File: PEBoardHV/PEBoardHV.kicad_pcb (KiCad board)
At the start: 2 copper layers, 106.7 x 76.7 mm, 44 parts, among them J1 To PE LV, J2 Left Connector (Master), J3 E-Meter Internal, J4 Right Connector (Slave), J5 E-Meter External, J6 HV Cable, J7 TSMPs, J8 HV CAN Debug, J9 EMeter HV, U1 L78S05CV-DG, U2 ISO1050, U3 PS2501-4, U4 DK1A1B-12V, U5 DK1A1B-12V

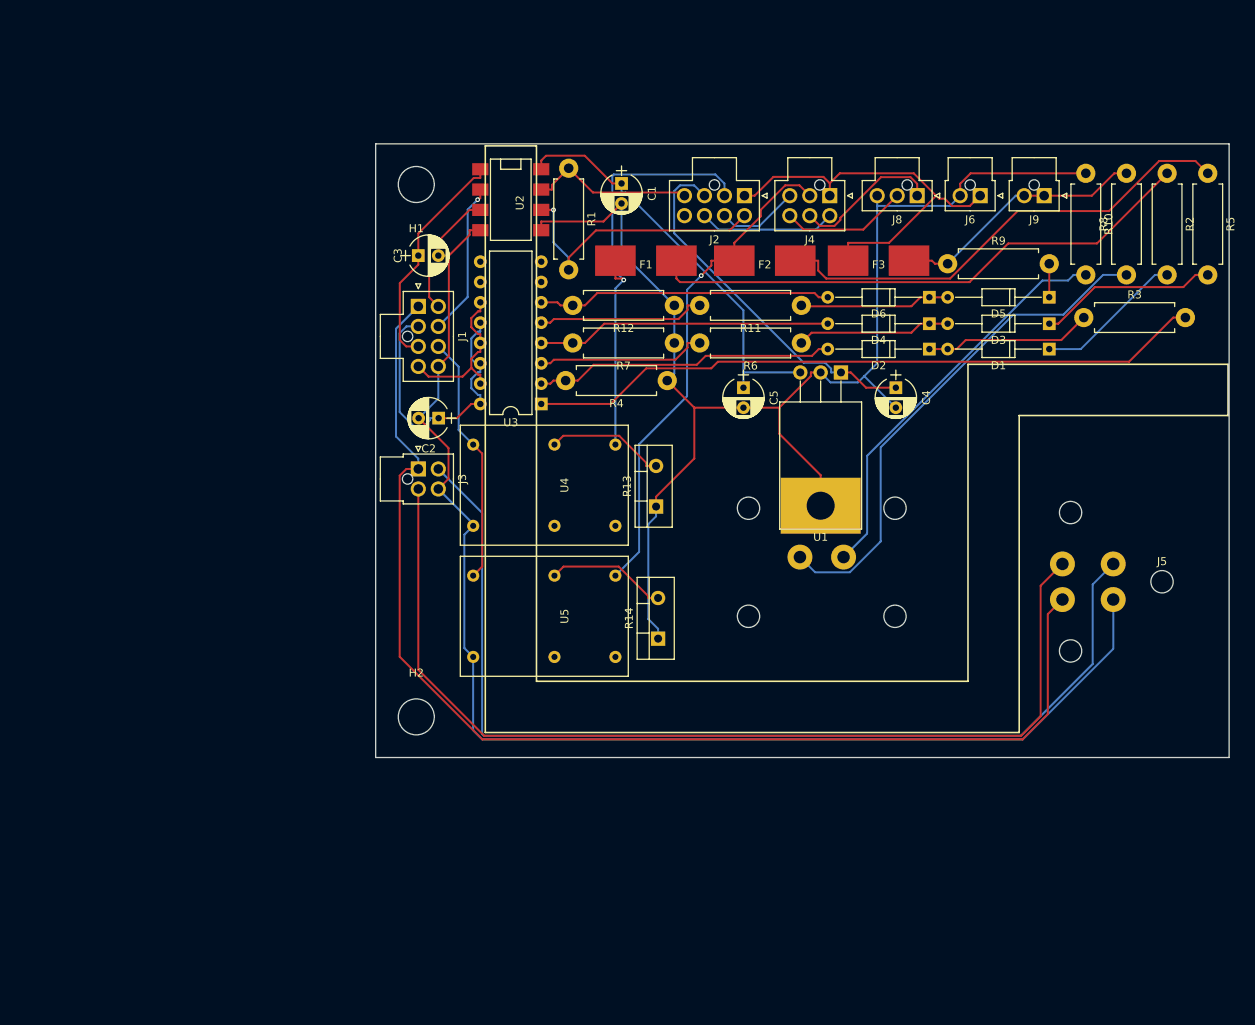
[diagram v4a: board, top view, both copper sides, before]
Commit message: Add ground planes to PE HV PCB and add an additional mounting hole
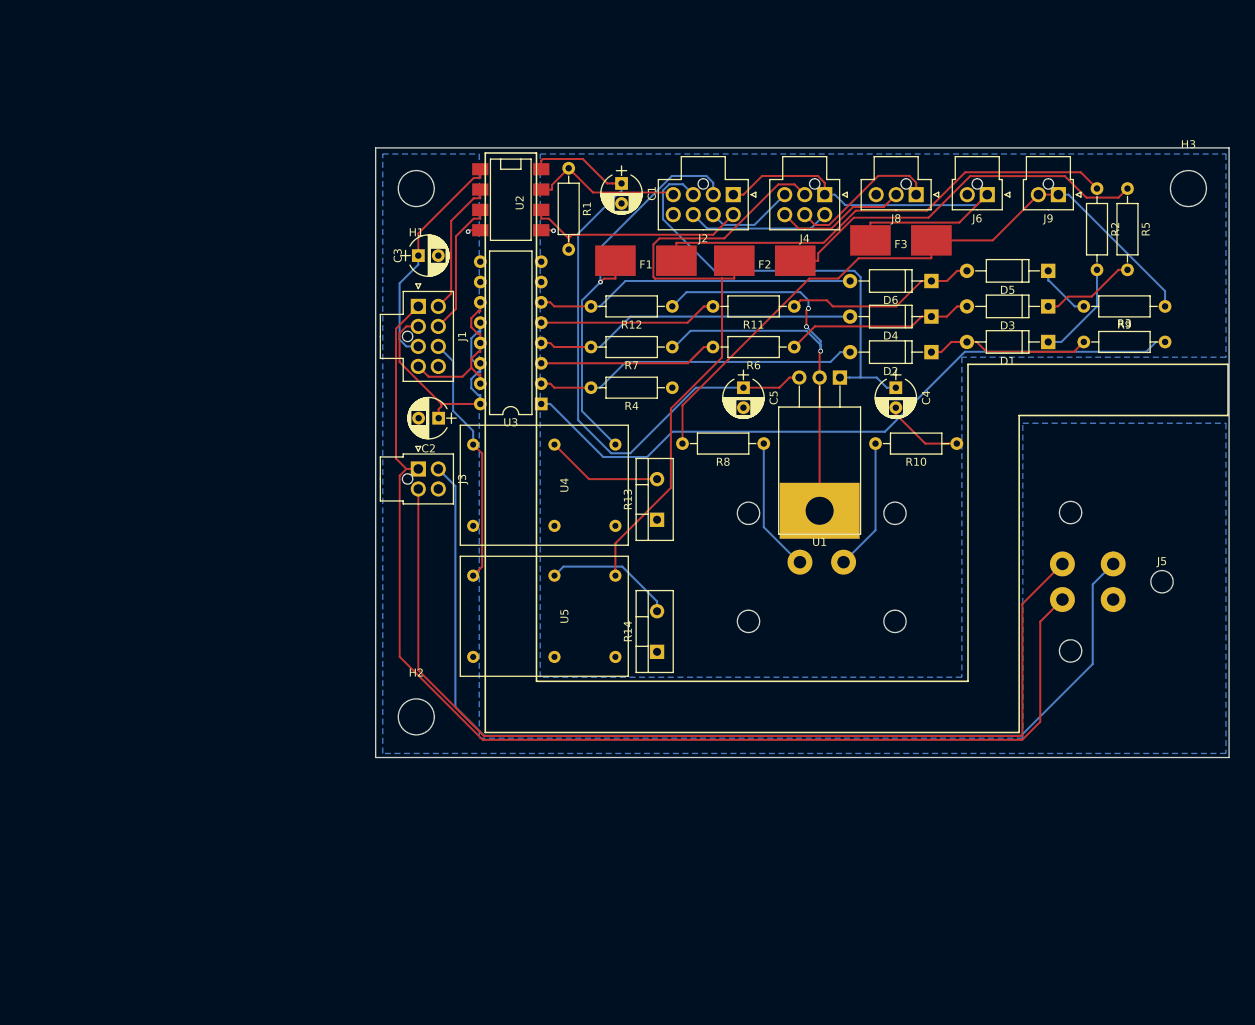
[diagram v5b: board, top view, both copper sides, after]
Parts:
- added H3: MtngHole, Mounting_Holes:MountingHole_4.5mm, F.Cu at (222.0, 56.4)
- D1, D2, D3, D4, D5, D6: footprint Diodes_THT:D_DO-35_SOD27_P12.70mm_Horizontal -> Diodes_THT:D_A-405_P10.16mm_Horizontal
- R1, R10, R11, R12, R2, R3, R4, R5, R6, R7, R8, R9: footprint Resistors_THT:R_Axial_DIN0411_L9.9mm_D3.6mm_P12.70mm_Horizontal -> Resistors_THT:R_Axial_DIN0207_L6.3mm_D2.5mm_P10.16mm_Horizontal
- moved R8 50.0 mm to (168.9, 88.3), turned to 180 degrees
- moved R10 37.4 mm to (193.0, 88.3), turned to 180 degrees
- moved R9 27.7 mm to (219.1, 71.1), turned to 180 degrees
- moved R5 10.2 mm to (214.4, 56.4)
- moved R2 8.97 mm to (210.6, 56.4)
- moved F3 3.78 mm to (186.1, 62.9)
- moved D5 3.30 mm to (204.5, 66.7)
- moved R3 3.05 mm to (208.9, 75.6)
- moved D3 2.16 mm to (204.5, 71.1)
- moved D6 2.05 mm to (189.9, 67.9)
- moved J9 1.78 mm to (205.7, 57.1)
- moved R13 1.66 mm to (155.6, 97.8)
- moved R14 1.66 mm to (155.6, 114.3)
- moved J2 1.40 mm to (165.1, 57.1)
- moved R4 1.09 mm to (157.5, 81.3)
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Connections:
- J1 pad 5: /CAN_TX -> /CAN_RX
- J1 pad 6: /CAN_RX -> /CAN_TX
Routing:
- net GND: track 163.9 -> 1.59 mm, vias 0 -> 1
- net /TS-: track 169.9 -> 77.8 mm, vias 0 -> 4
- net /TS+_FUSED: track 32.0 -> 84.2 mm
- net Net-(J7-Pad1): track 63.9 -> 16.8 mm
- net Net-(J7-Pad2): track 50.6 -> 16.5 mm
- net /5V_TS: track 52.1 -> 77.8 mm
- net /TS+_SWITCHED_R: track 62.9 -> 81.7 mm, vias 1 -> 0
- net Net-(F2-Pad2): track 59.9 -> 48.0 mm
- net Net-(D3-Pad1): track 22.3 -> 11.8 mm
- net /CAN+: track 45.9 -> 56.0 mm
- net Net-(F1-Pad2): track 69.4 -> 59.3 mm
- net /CAN_L_BOARD: track 35.5 -> 28.7 mm, vias 1 -> 0
- net Net-(D1-Pad1): track 18.6 -> 12.5 mm
- net Net-(D5-Pad2): track 18.8 -> 24.1 mm
- net Net-(D3-Pad2): track 19.3 -> 23.7 mm
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- added copper zone on B.Cu, net /TS-
- added copper zone on B.Cu, net GND
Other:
- board size 106.7 x 76.7 mm -> 106.7 x 76.2 mm

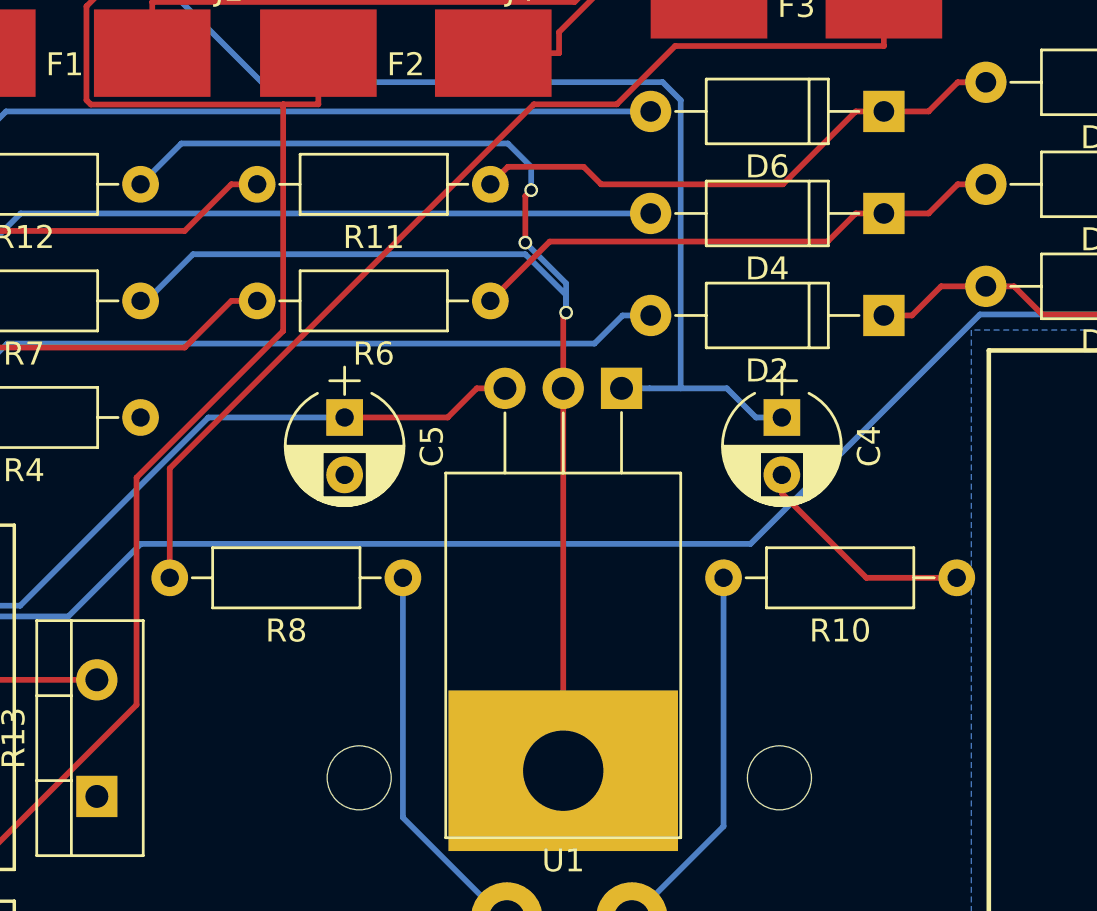
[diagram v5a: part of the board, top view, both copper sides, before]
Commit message: Fix via size for manufacturing
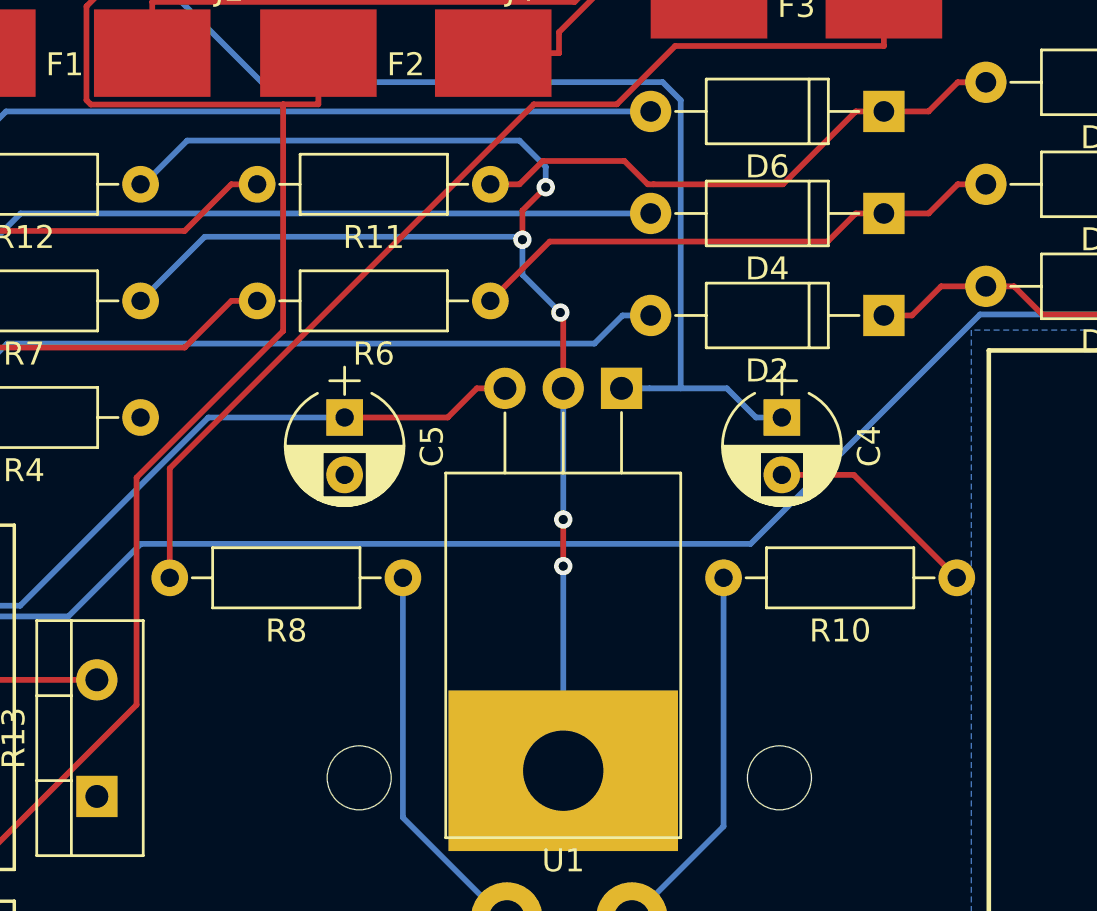
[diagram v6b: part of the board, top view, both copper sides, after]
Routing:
- net /TS-: track 77.8 -> 75.3 mm, vias 4 -> 6
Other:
- net class Default: via_dia 0.6 -> 0.8
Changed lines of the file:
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@@
     (links 85)
     (no_connects 0)
-    (area 120.345999 50.749999 227.126001 127.558001)
+    (area 120.345999 49.913 227.349001 129.003)
     (thickness 1.6)
     (drawings 14)
-    (tracks 328)
+    (tracks 332)
     (zones 0)
     (modules 45)
@@
     (segment_width 0.2)
     (edge_width 0.1)
-    (via_size 0.6)
+    (via_size 0.8)
     (via_drill 0.4)
     (via_min_size 0.4)
@@
     (clearance 0.2)
     (trace_width 0.25)
-    (via_dia 0.6)
+    (via_dia 0.8)
     (via_drill 0.4)
     (uvia_dia 0.3)
@@
   (segment (start 184.2947 81.28) (end 183.0247 80.01) (width 0.25) (layer B.Cu) (net 4))
   (segment (start 181.0133 80.01) (end 179.6603 80.01) (width 0.25) (layer B.Cu) (net 4))
-  (segment (start 157.48 71.12) (end 159.258 69.342) (width 0.25) (layer B.Cu) (net 5))
-  (segment (start 176.022 75.438) (end 176.022 76.708) (width 0.25) (layer B.Cu) (net 5))
-  (segment (start 174.244 73.66) (end 176.022 75.438) (width 0.25) (layer B.Cu) (net 5))
-  (via (at 174.244 73.66) (size 0.6) (drill 0.4) (layers F.Cu B.Cu) (net 5))
-  (segment (start 174.244 71.628) (end 174.244 73.66) (width 0.25) (layer F.Cu) (net 5))
-  (segment (start 174.498 71.374) (end 174.244 71.628) (width 0.25) (layer F.Cu) (net 5))
-  (via (at 174.498 71.374) (size 0.6) (drill 0.4) (layers F.Cu B.Cu) (net 5))
-  (segment (start 174.498 70.358) (end 174.498 71.374) (width 0.25) (layer B.Cu) (net 5))
-  (segment (start 173.482 69.342) (end 174.498 70.358) (width 0.25) (layer B.Cu) (net 5))
-  (segment (start 159.258 69.342) (end 173.482 69.342) (width 0.25) (layer B.Cu) (net 5))
-  (segment (start 157.48 76.2) (end 157.734 76.2) (width 0.25) (layer B.Cu) (net 5))
-  (segment (start 157.734 76.2) (end 159.766 74.168) (width 0.25) (layer B.Cu) (net 5))
-  (segment (start 159.766 74.168) (end 174.244 74.168) (width 0.25) (layer B.Cu) (net 5))
-  (segment (start 174.244 74.168) (end 176.022 75.946) (width 0.25) (layer B.Cu) (net 5))
-  (segment (start 176.022 75.946) (end 176.022 76.708) (width 0.25) (layer B.Cu) (net 5))
-  (via (at 176.022 76.708) (size 0.6) (drill 0.4) (layers F.Cu B.Cu) (net 5))
-  (segment (start 176.022 76.708) (end 175.895 76.835) (width 0.25) (layer F.Cu) (net 5))
-  (segment (start 175.895 76.835) (end 175.895 80.01) (width 0.25) (layer F.Cu) (net 5))
-  (segment (start 175.895 80.01) (end 175.895 96.67) (width 0.25) (layer F.Cu) (net 5))
-  (segment (start 185.42 83.78) (end 185.42 84.582) (width 0.25) (layer F.Cu) (net 5))
-  (segment (start 189.103 88.265) (end 193.04 88.265) (width 0.25) (layer F.Cu) (net 5))
-  (segment (start 185.42 84.582) (end 189.103 88.265) (width 0.25) (layer F.Cu) (net 5))
+  (segment (start 175.895 80.01) (end 175.895 76.835) (width 0.25) (layer F.Cu) (net 5) (status 400000))
+  (segment (start 174.117 75.057) (end 174.117 73.533) (width 0.25) (layer B.Cu) (net 5))
+  (segment (start 175.768 76.708) (end 174.117 75.057) (width 0.25) (layer B.Cu) (net 5))
+  (via (at 175.768 76.708) (size 0.8) (drill 0.4) (layers F.Cu B.Cu) (net 5))
+  (segment (start 175.895 76.835) (end 175.768 76.708) (width 0.25) (layer F.Cu) (net 5))
+  (segment (start 157.48 71.12) (end 157.607 71.12) (width 0.25) (layer B.Cu) (net 5) (status C00000))
+  (segment (start 157.607 71.12) (end 159.512 69.215) (width 0.25) (layer B.Cu) (net 5) (status 400000))
+  (via (at 174.117 73.533) (size 0.8) (drill 0.4) (layers F.Cu B.Cu) (net 5))
+  (segment (start 174.117 72.263) (end 174.117 73.533) (width 0.25) (layer F.Cu) (net 5))
+  (segment (start 175.133 71.247) (end 174.117 72.263) (width 0.25) (layer F.Cu) (net 5))
+  (via (at 175.133 71.247) (size 0.8) (drill 0.4) (layers F.Cu B.Cu) (net 5))
+  (segment (start 175.133 70.358) (end 175.133 71.247) (width 0.25) (layer B.Cu) (net 5))
+  (segment (start 173.99 69.215) (end 175.133 70.358) (width 0.25) (layer B.Cu) (net 5))
+  (segment (start 159.512 69.215) (end 173.99 69.215) (width 0.25) (layer B.Cu) (net 5))
+  (segment (start 174.117 73.533) (end 173.99 73.406) (width 0.25) (layer B.Cu) (net 5))
+  (segment (start 160.274 73.406) (end 157.48 76.2) (width 0.25) (layer B.Cu) (net 5) (status 800000))
+  (segment (start 173.99 73.406) (end 160.274 73.406) (width 0.25) (layer B.Cu) (net 5))
+  (segment (start 175.895 96.67) (end 175.895 87.757) (width 0.25) (layer B.Cu) (net 5) (status 400000))
+  (segment (start 175.895 85.725) (end 175.895 80.01) (width 0.25) (layer B.Cu) (net 5) (status 800000))
+  (via (at 175.895 85.725) (size 0.8) (drill 0.4) (layers F.Cu B.Cu) (net 5))
+  (segment (start 175.895 87.757) (end 175.895 85.725) (width 0.25) (layer F.Cu) (net 5))
+  (via (at 175.895 87.757) (size 0.8) (drill 0.4) (layers F.Cu B.Cu) (net 5))
+  (segment (start 185.42 83.78) (end 188.555 83.78) (width 0.25) (layer F.Cu) (net 5) (status 400000))
+  (segment (start 188.555 83.78) (end 193.04 88.265) (width 0.25) (layer F.Cu) (net 5) (status 800000))
   (via (at 142.6362 61.6604) (size 0.6) (layers F.Cu B.Cu) (net 5))
   (segment (start 141.097 61.595) (end 142.4383 61.595) (width 0.25) (layer F.Cu) (net 5))
@@
   (segment (start 208.915 71.12) (end 207.7897 71.12) (width 0.25) (layer B.Cu) (net 13))
   (segment (start 204.47 66.675) (end 204.47 67.9003) (width 0.25) (layer B.Cu) (net 13))
-  (segment (start 172.72 71.12) (end 173.482 70.358) (width 0.25) (layer F.Cu) (net 14))
-  (segment (start 176.784 70.358) (end 177.546 71.12) (width 0.25) (layer F.Cu) (net 14))
-  (segment (start 173.482 70.358) (end 176.784 70.358) (width 0.25) (layer F.Cu) (net 14))
+  (segment (start 173.99 71.12) (end 175.006 70.104) (width 0.25) (layer F.Cu) (net 14))
+  (segment (start 179.578 71.12) (end 179.832 71.12) (width 0.25) (layer F.Cu) (net 14))
+  (segment (start 178.562 70.104) (end 179.578 71.12) (width 0.25) (layer F.Cu) (net 14))
+  (segment (start 175.006 70.104) (end 178.562 70.104) (width 0.25) (layer F.Cu) (net 14))
   (segment (start 191.8147 67.945) (end 193.0847 66.675) (width 0.25) (layer F.Cu) (net 14))
   (segment (start 189.865 67.945) (end 191.8147 67.945) (width 0.25) (layer F.Cu) (net 14))
   (segment (start 194.31 66.675) (end 193.0847 66.675) (width 0.25) (layer F.Cu) (net 14))
   (segment (start 185.4647 71.12) (end 188.6397 67.945) (width 0.25) (layer F.Cu) (net 14))
-  (segment (start 177.546 71.12) (end 185.4647 71.12) (width 0.25) (layer F.Cu) (net 14))
+  (segment (start 172.72 71.12) (end 173.99 71.12) (width 0.25) (layer F.Cu) (net 14))
+  (segment (start 179.832 71.12) (end 185.4647 71.12) (width 0.25) (layer F.Cu) (net 14))
   (segment (start 189.865 67.945) (end 188.6397 67.945) (width 0.25) (layer F.Cu) (net 14))
   (segment (start 142.7303 71.12) (end 142.2223 70.612) (width 0.25) (layer F.Cu) (net 15))
